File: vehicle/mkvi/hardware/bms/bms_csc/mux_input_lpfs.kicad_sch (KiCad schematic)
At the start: 2 parts

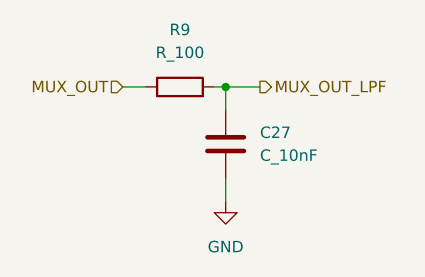
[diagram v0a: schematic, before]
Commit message: Removed I2C PU resistors bc already on DA board
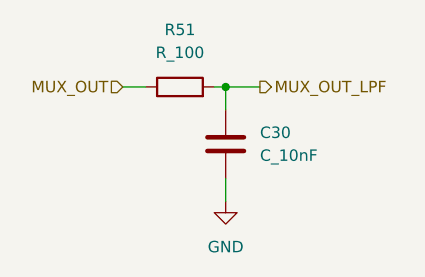
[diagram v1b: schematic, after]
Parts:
- renumbered C27 to C30, R9 to R51
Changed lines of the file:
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@@
 		(dnp no)
 		(fields_autoplaced yes)
-		(property "Reference" "C27"
+		(property "Reference" "C30"
 			(at 152.4 83.8199 0)
 			(effects
@@
 		(dnp no)
 		(fields_autoplaced yes)
-		(property "Reference" "R9"
+		(property "Reference" "R51"
 			(at 143.51 72.39 90)
 			(effects
